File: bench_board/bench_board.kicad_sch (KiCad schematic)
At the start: 61 parts, among them J1 BATT_4S, J10 BUZZER, J2 BOOT0_JUMPER, J3 USB-C, J4 CRSF_UART, J5 DSHOT_M1-M4, J6 SWD, J7 RX_PWR_5V, J8 TELEM_TX, J9 EXPANSION_BUS, Q1 AO3400A, U1 STM32F405RGT6, U2 TPS54336ADDA, U4 MPU-6000, U5 USBLC6-2SC6, U6 MT3608, Y1 8MHz

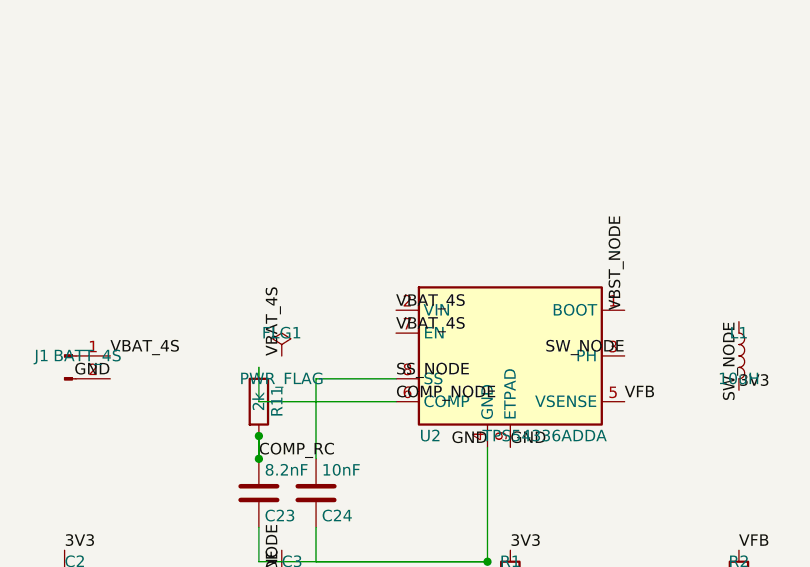
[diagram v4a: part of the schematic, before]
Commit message: Item 1: EN abs-max violation fixed -- TI Figure-15 UVLO divider, EN never above 2.6V
THE ARITHMETIC (from SLVSCD5D Eq. 2/3 with the device's own numbers:
Ip=1.15uA, Ih=3.3uA, VENrising=1.21V, VENfalling=1.17V):
targets Vstart=12.0V, Vstop=11.0V give R1=180.74k, R2=19.89k exact;
fitted E96 pair R16=182k (LCSC C11481, Extended -- no Basic exists at
180k/182k 0402), R17=20k (C25765, Basic). Realized thresholds:
  START (rising)  = 1.21*(1+182/20) - 1.15uA*182k = 12.012V (3.003V/cell)
  STOP  (falling) = 1.17*(1+182/20) - 4.45uA*182k = 11.007V (2.752V/cell)
  hysteresis 1.005V (datasheet recommends >500mV)
EN pin voltage (divider + (Ip+Ih)*R1||R2): 1.27V @12V, 1.74V @16.8V,
2.58V @25.2V -- all far under the 6V abs-max at every corner including
6S. Idle divider drain 83uA from the pack.

Schematic: EN label on U2.7 renamed to EN_UVLO; R16 VBAT_4S->EN_UVLO,
R17 EN_UVLO->GND; ERC 0. Netlist verified: /EN_UVLO = {U2.7, R16.2,
R17.1} exactly; EN removed from /VBAT_4S.

Board: old EN spur (4 segments C1.1 -> pad 7) deleted; R16/R17 placed
at (21.25,41.85)/(23.15,41.7) in the strip south of C1; VBAT tap into
C1.1; EN runs R16.P2 -> short F.Cu stub -> B.Cu (empty there) ->
via -> F.Cu -> U2.7, dodging the COMP via, L1 pads, and MH3's 6mm
mask aperture (an F.Cu corner at (21.8,44.7) turned out to poke 0.15mm
into that aperture and lit up 6 solder-mask-bridge violations -- the
B.Cu detour exists because F.Cu is walled by the GND highway at
y=40.86, C1, L1, and that aperture). R17 GND taps the existing 0.6mm
GND trace at y=40.86 -- no new GND via needed. Two new 0.6/0.3 EN
vias; the one at (21.76,42.1) overlaps R16's own EN pad edge -- add it
to the filled-and-capped list.

Guard: 53 violations / 2 unconnected / 95 parity. Violations AT
baseline; unconnected = the two known bench-jumper pads; parity +2 is
exactly the two new footprints' empty-field mismatches (same class as
the existing 61). Baseline re-recorded at 53/2/95 with this
justification. Planes refilled with KiCad's own 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
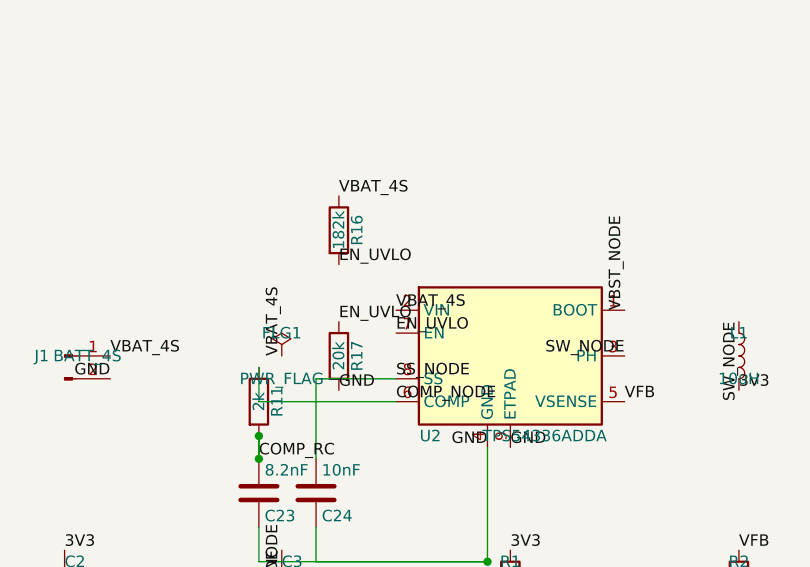
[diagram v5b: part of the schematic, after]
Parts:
- added R16: 182k, Resistor_SMD:R_0402_1005Metric, symbol Device:R
- added R17: 20k, Resistor_SMD:R_0402_1005Metric, symbol Device:R
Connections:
- net GND: now also R17.2
- net VBAT_4S: now also R16.1; no longer U2.7 (EN)
- new net EN_UVLO: R16.2, R17.1, U2.7 (EN)
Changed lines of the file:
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@@
-		)
-	)
-	(label "VBAT_4S"
-		(at 387.35 46.99 0)
-		(effects
-			(font
-				(size 1.27 1.27)
-			)
-			(justify left bottom)
 		)
 	)
@@
 		(effects
 			(font
+				(size 1.27 1.27)
+			)
+			(justify left bottom)
+		)
+	)
+	(label "EN_UVLO"
+		(at 387.35 46.99 0)
+		(effects
+			(font
+				(size 1.27 1.27)
+			)
+			(justify left bottom)
+		)
+	)
+	(symbol
+		(lib_id "Device:R")
+		(at 381 35.56 0)
+		(unit 1)
+		(body_style 1)
+		(exclude_from_sim no)
+		(in_bom yes)
+		(on_board yes)
+		(in_pos_files yes)
+		(dnp no)
+		(property "Reference" "R16"
+			(at 383.032 35.56 90)
+			(show_name no)
+			(do_not_autoplace no)
+			(effects
+				(font
+					(size 1.27 1.27)
+				)
+			)
+		)
+		(property "Value" "182k"
+			(at 381 35.56 90)
+			(show_name no)
+			(do_not_autoplace no)
+			(effects
+				(font
+					(size 1.27 1.27)
+				)
+			)
+		)
+		(property "Footprint" "Resistor_SMD:R_0402_1005Metric"
+			(at 379.222 35.56 90)
+			(hide yes)
+			(show_name no)
+			(do_not_autoplace no)
+			(effects
+				(font
+					(size 1.27 1.27)
+				)
+			)
+		)
+		(property "Datasheet" ""
+			(at 381 35.56 0)
+			(hide yes)
+			(show_name no)
+			(do_not_autoplace no)
+			(effects
+				(font
+					(size 1.27 1.27)
+				)
+			)
+		)
+		(property "Description" "Resistor"
+			(at 381 35.56 0)
+			(hide yes)
+			(show_name no)
+			(do_not_autoplace no)
+			(effects
+				(font
+					(size 1.27 1.27)
+				)
+			)
+		)
+		(pin "1"
+		)
+		(pin "2"
+		)
+		(instances
+			(project "bench_board"
+				(path "/b1d50a66-1761-4ba7-abb7-c1970eec7e0d"
+					(reference "R16")
+					(unit 1)
+				)
+			)
+		)
+	)
+	(symbol
+		(lib_id "Device:R")
+		(at 381 49.53 0)
+		(unit 1)
+		(body_style 1)
+		(exclude_from_sim no)
+		(in_bom yes)
+		(on_board yes)
+		(in_pos_files yes)
+		(dnp no)
+		(property "Reference" "R17"
+			(at 383.032 49.53 90)
+			(show_name no)
+			(do_not_autoplace no)
+			(effects
+				(font
+					(size 1.27 1.27)
+				)
+			)
+		)
+		(property "Value" "20k"
+			(at 381 49.53 90)
+			(show_name no)
+			(do_not_autoplace no)
+			(effects
+				(font
+					(size 1.27 1.27)
+				)
+			)
+		)
+		(property "Footprint" "Resistor_SMD:R_0402_1005Metric"
+			(at 379.222 49.53 90)
+			(hide yes)
+			(show_name no)
+			(do_not_autoplace no)
+			(effects
+				(font
+					(size 1.27 1.27)
+				)
+			)
+		)
+		(property "Datasheet" ""
+			(at 381 49.53 0)
+			(hide yes)
+			(show_name no)
+			(do_not_autoplace no)
+			(effects
+				(font
+					(size 1.27 1.27)
+				)
+			)
+		)
+		(property "Description" "Resistor"
+			(at 381 49.53 0)
+			(hide yes)
+			(show_name no)
+			(do_not_autoplace no)
+			(effects
+				(font
+					(size 1.27 1.27)
+				)
+			)
+		)
+		(pin "1"
+		)
+		(pin "2"
+		)
+		(instances
+			(project "bench_board"
+				(path "/b1d50a66-1761-4ba7-abb7-c1970eec7e0d"
+					(reference "R17")
+					(unit 1)
+				)
+			)
+		)
+	)
+	(label "VBAT_4S"
+		(at 381.0 31.750000000000004 0)
+		(effects
+			(font
+				(size 1.27 1.27)
+			)
+			(justify left bottom)
+		)
+	)
+	(label "EN_UVLO"
+		(at 381.0 39.370000000000005 0)
+		(effects
+			(font
+				(size 1.27 1.27)
+			)
+			(justify left bottom)
+		)
+	)
+	(label "EN_UVLO"
+		(at 381.0 45.72 0)
+		(effects
+			(font
+				(size 1.27 1.27)
+			)
+			(justify left bottom)
+		)
+	)
+	(label "GND"
+		(at 381.0 53.34 0)
+		(effects
+			(font

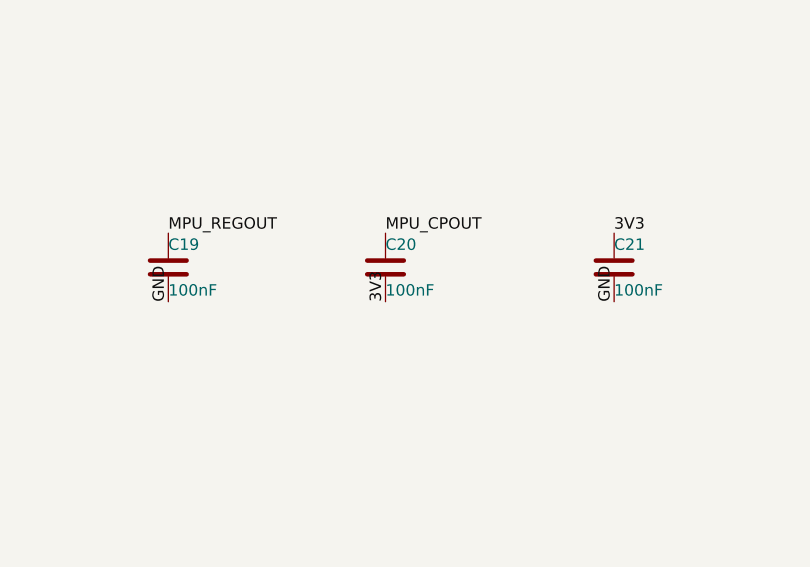
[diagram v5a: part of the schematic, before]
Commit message: Item 2: MPU-6000 charge-pump cap fixed on all three axes -- 2.2nF, 50V part, returned to GND
Per PS-MPU-6000A section 7.3: CPOUT capacitor must be 2.2nF X7R 50V to
GND; the board had 100nF/16V to 3V3. Schematic: C20 pin-2 label 3V3 ->
GND, value 100nF -> 2.2nF; ERC 0; netlist verified /MPU_CPOUT =
{C20.1, U4.20} and C20.2 now in /GND. Part: Yageo CC0402KRX7R9BB222,
LCSC C106861 (X7R 50V, 1.14M stock) -- no Basic-library 2.2nF/50V 0402
exists, so this is one more Extended fee, said plainly.

Board: pad 2 renet to /GND; the two 3V3 feeder segments deleted (C21.1
keeps its feed from the far side -- verified the chain is fed from
(44.708,34.932), not through C20); new 0.3mm GND return east-then-north
to the existing 0.8/0.4 GND via at (45.753,29.452), dodging C20's own
CPOUT pad (first attempt clipped it at 0.17mm -- caught by the guard,
rerouted) and the CPOUT via. No new vias.

CONSEQUENCE FOR THE ORDER SHEET (picked up in item 4): the U1.48 bench
jumper's documented target was C20 pad 2 *because it was 3V3*. It is
GND now. New target: C21 pad 1 (45.599,34.041), /3V3, 9.2mm from pad
48.

Guard: PASS 53/2/95, unchanged from the item-1 baseline. Planes
refilled, 4/4 coherent.

Co-Authored-By: Claude Fable 5 <noreply@anthropic.com>
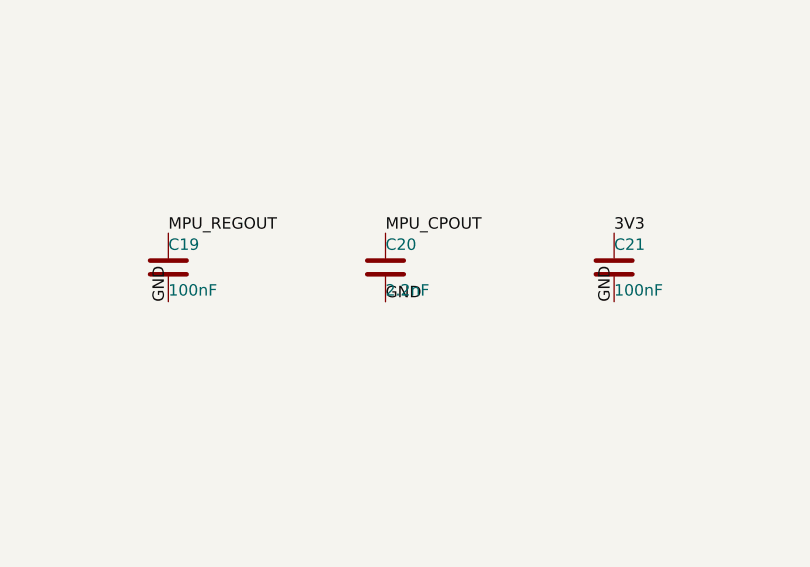
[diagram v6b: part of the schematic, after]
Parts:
- C20: value 100nF -> 2.2nF
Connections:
- net 3V3: no longer C20.2
- net GND: now also C20.2
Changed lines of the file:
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@@
 			)
 		)
-		(property "Value" "100nF"
+		(property "Value" "2.2nF"
 			(at 444.5 273.05 0)
 			(show_name no)
@@
 	)
 	(label "3V3"
-		(at 444.5 274.32 90)
-		(effects
-			(font
-				(size 1.27 1.27)
-			)
-			(justify left bottom)
-		)
-	)
-	(label "3V3"
 		(at 469.9 266.7 0)
 		(effects
@@
 		(effects
 			(font
+				(size 1.27 1.27)
+			)
+			(justify left bottom)
+		)
+	)
+	(label "GND"
+		(at 444.5 274.32 0)
+		(effects
+			(font
